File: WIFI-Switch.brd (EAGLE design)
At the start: 31.8 x 67.8 mm, 23 parts, among them T1 BT136/138/139, U1 AMS1117

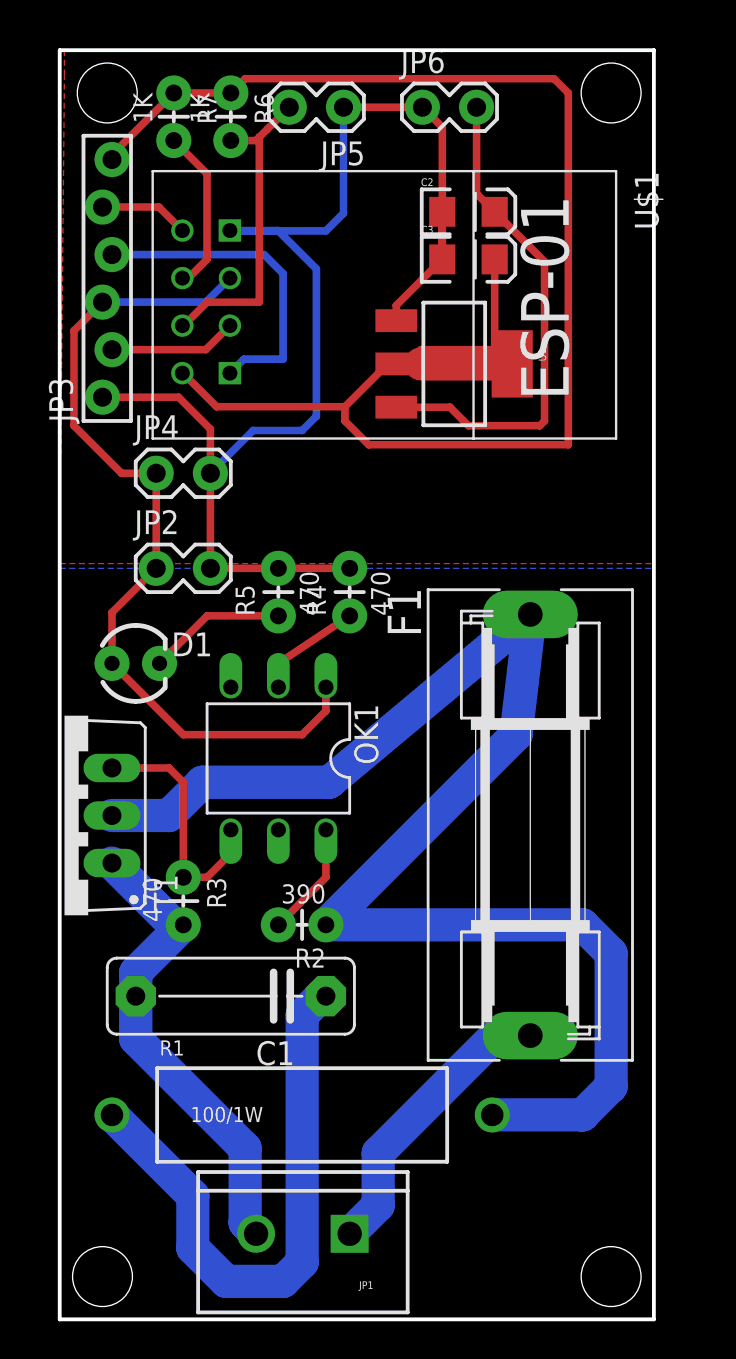
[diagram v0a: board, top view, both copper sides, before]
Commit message: update board size
update board size and components reposition
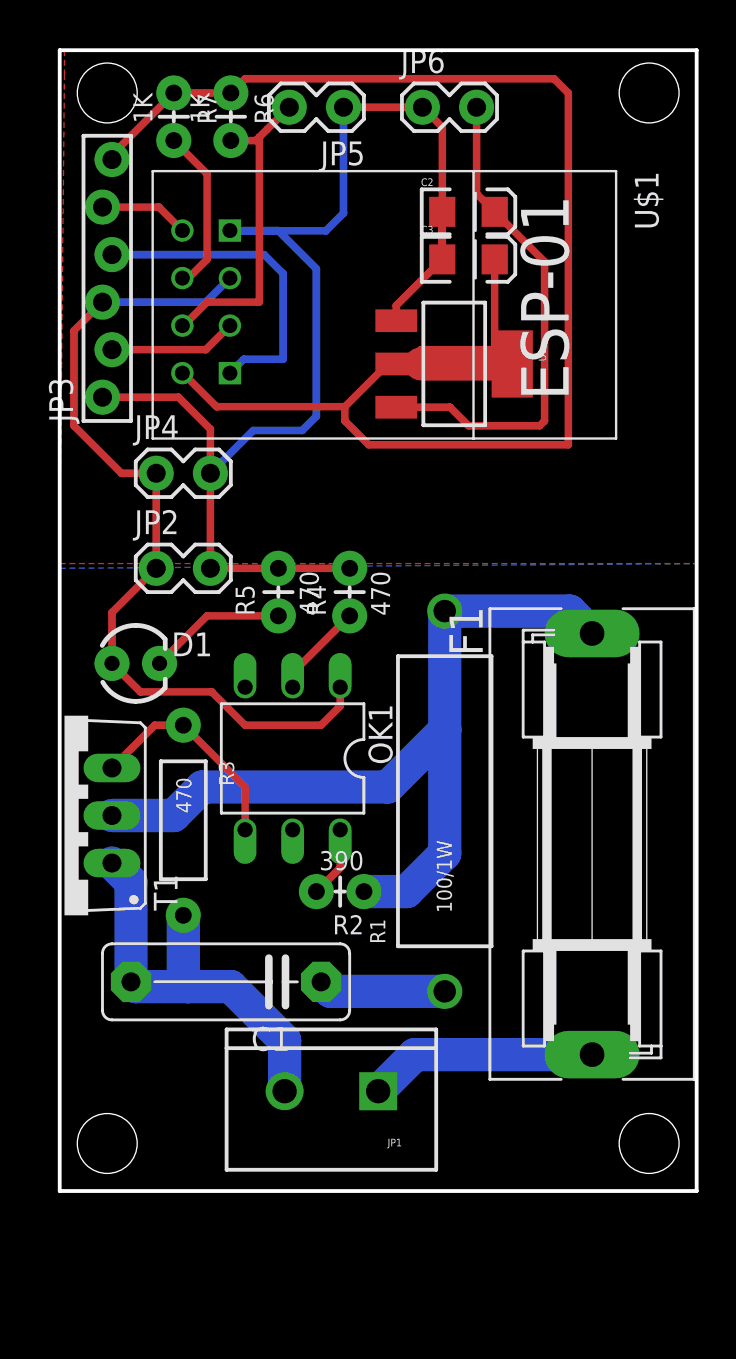
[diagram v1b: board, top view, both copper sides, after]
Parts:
- R3: device SparkFun-Resistors:AXIAL-0.1 -> SparkFun-Resistors:AXIAL-0.4
- moved R1 18.4 mm to (20.3, 62.5), turned to 90 degrees
- moved JP1 7.77 mm to (16.8, 47.0)
- moved F1 3.45 mm to (28.2, 60.2)
- moved R3 3.05 mm to (6.35, 61.5)
- moved R2 2.70 mm to (16.0, 57.7)
- moved C1 0.80 mm to (8.64, 52.8)
- moved OK1 0.76 mm to (12.2, 64.8)
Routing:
- net N$20: track 77.1 -> 46.2 mm
- net N$23: track 30.8 -> 6.81 mm
- net N$1: track 15.7 -> 12.2 mm
- net N$22: track 25.4 -> 22.9 mm
- net N$19: track 6.13 -> 3.83 mm
- net N$21: track 13.5 -> 11.7 mm
- net N$6: track 5.85 -> 5.07 mm
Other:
- board size 31.8 x 67.8 mm -> 34 x 61 mm
